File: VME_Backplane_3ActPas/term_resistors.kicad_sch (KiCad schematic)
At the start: 41 parts, among them X2H1 HI_L, X2L1 LO_L, X3H1 HI_R, X3L1 LO_R

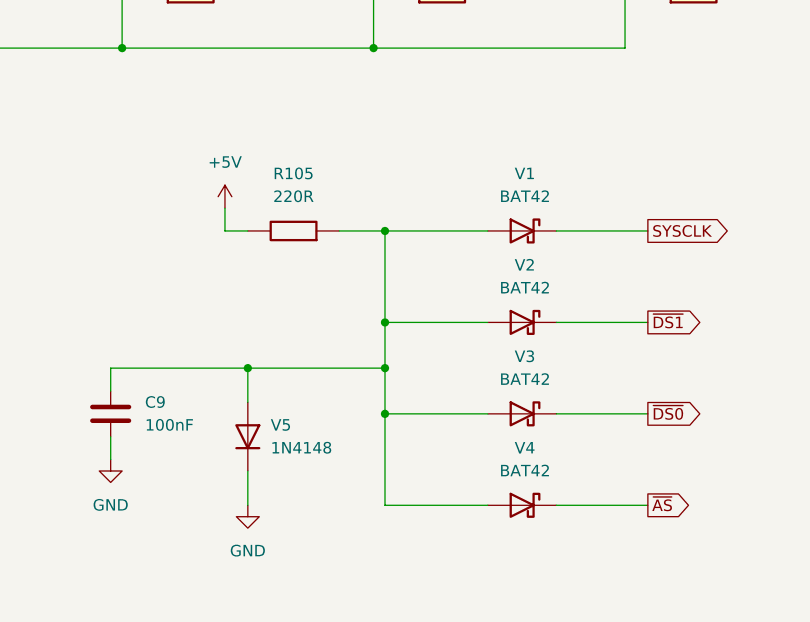
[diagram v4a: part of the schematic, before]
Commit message: Update resistor footprints with preferred silkscreen outlines
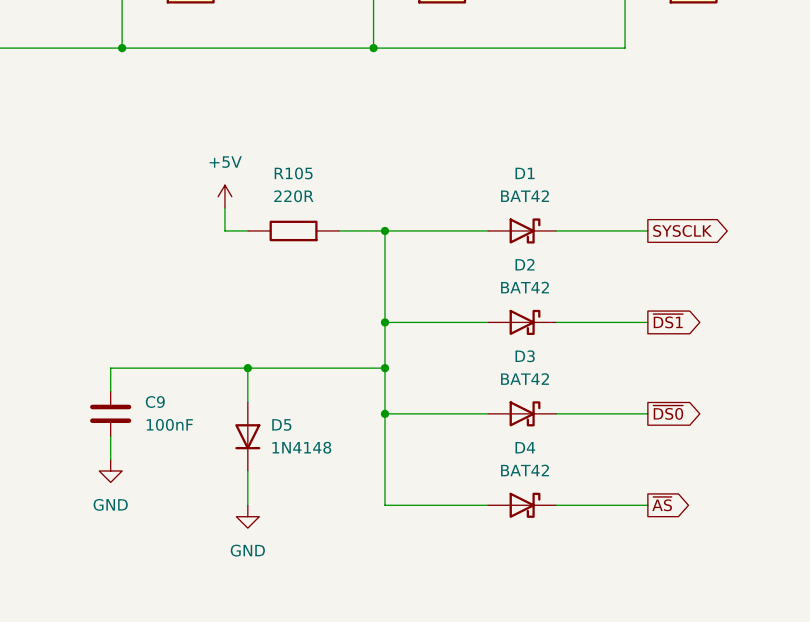
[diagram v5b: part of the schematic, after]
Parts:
- R1, R10, R11, R12, R13, R14, R15, R16, R17, R18, R2, R3, R4, R5, R6, R7, R8, R9: footprint Resistor_THT:R_Array_SIP10 -> COMET footprints:R_Array_SIP10
- R105: footprint Resistor_THT:R_Axial_DIN0207_L6.3mm_D2.5mm_P10.16mm_Horizontal -> COMET footprints:R_Axial_DIN0207_L6.3mm_D2.5mm_P10.16mm_Horizontal
- renumbered V1 to D1, V2 to D2, V3 to D3, V4 to D4, V5 to D5
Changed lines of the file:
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@@
     (property "Reference" "R14" (id 0) (at 144.78 68.58 90))
     (property "Value" "330R/470R" (id 1) (at 144.78 71.12 90))
-    (property "Footprint" "Resistor_THT:R_Array_SIP10" (id 2) (at 144.78 86.36 0)
+    (property "Footprint" "COMET footprints:R_Array_SIP10" (id 2) (at 144.78 86.36 0)
       (effects (font (size 1.27 1.27)) hide)
     )
@@
     (property "Reference" "R18" (id 0) (at 256.54 68.58 90))
     (property "Value" "330R/470R" (id 1) (at 256.54 71.12 90))
-    (property "Footprint" "Resistor_THT:R_Array_SIP10" (id 2) (at 256.54 86.36 0)
+    (property "Footprint" "COMET footprints:R_Array_SIP10" (id 2) (at 256.54 86.36 0)
       (effects (font (size 1.27 1.27)) hide)
     )
@@
     (property "Reference" "R12" (id 0) (at 88.9 68.58 90))
     (property "Value" "330R/470R" (id 1) (at 88.9 71.12 90))
-    (property "Footprint" "Resistor_THT:R_Array_SIP10" (id 2) (at 88.9 86.36 0)
+    (property "Footprint" "COMET footprints:R_Array_SIP10" (id 2) (at 88.9 86.36 0)
       (effects (font (size 1.27 1.27)) hide)
     )
@@
     (property "Reference" "R3" (id 0) (at 88.9 22.86 90))
     (property "Value" "330R/470R" (id 1) (at 88.9 25.4 90))
-    (property "Footprint" "Resistor_THT:R_Array_SIP10" (id 2) (at 88.9 40.64 0)
+    (property "Footprint" "COMET footprints:R_Array_SIP10" (id 2) (at 88.9 40.64 0)
       (effects (font (size 1.27 1.27)) hide)
     )
@@
   (symbol (lib_id "Diode:BAT42") (at 237.49 152.4 0) (mirror y) (unit 1)
     (in_bom yes) (on_board yes) (fields_autoplaced)
-    (property "Reference" "V4" (id 0) (at 237.8075 146.05 0))
+    (property "Reference" "D4" (id 0) (at 237.8075 146.05 0))
     (property "Value" "BAT42" (id 1) (at 237.8075 148.59 0))
     (property "Footprint" "Diode_THT:D_DO-35_SOD27_P10.16mm_Horizontal" (id 2) (at 237.49 156.845 0)
@@
     (property "Reference" "R5" (id 0) (at 144.78 22.86 90))
     (property "Value" "330R/470R" (id 1) (at 144.78 25.4 90))
-    (property "Footprint" "Resistor_THT:R_Array_SIP10" (id 2) (at 144.78 40.64 0)
+    (property "Footprint" "COMET footprints:R_Array_SIP10" (id 2) (at 144.78 40.64 0)
       (effects (font (size 1.27 1.27)) hide)
     )
@@
     (property "Reference" "R16" (id 0) (at 200.66 68.58 90))
     (property "Value" "330R/470R" (id 1) (at 200.66 71.12 90))
-    (property "Footprint" "Resistor_THT:R_Array_SIP10" (id 2) (at 200.66 86.36 0)
+    (property "Footprint" "COMET footprints:R_Array_SIP10" (id 2) (at 200.66 86.36 0)
       (effects (font (size 1.27 1.27)) hide)
     )
@@
     (property "Reference" "R105" (id 0) (at 212.09 115.57 90))
     (property "Value" "220R" (id 1) (at 212.09 118.11 90))
-    (property "Footprint" "Resistor_THT:R_Axial_DIN0207_L6.3mm_D2.5mm_P10.16mm_Horizontal" (id 2) (at 212.09 121.92 0)
+    (property "Footprint" "COMET footprints:R_Axial_DIN0207_L6.3mm_D2.5mm_P10.16mm_Horizontal" (id 2) (at 212.09 121.92 0)
       (effects (font (size 1.27 1.27)) hide)
     )
@@
     (property "Reference" "R4" (id 0) (at 116.84 22.86 90))
     (property "Value" "330R/470R" (id 1) (at 116.84 25.4 90))
-    (property "Footprint" "Resistor_THT:R_Array_SIP10" (id 2) (at 116.84 40.64 0)
+    (property "Footprint" "COMET footprints:R_Array_SIP10" (id 2) (at 116.84 40.64 0)
       (effects (font (size 1.27 1.27)) hide)
     )
@@
     (property "Reference" "R6" (id 0) (at 172.72 22.86 90))
     (property "Value" "330R/470R" (id 1) (at 172.72 25.4 90))
-    (property "Footprint" "Resistor_THT:R_Array_SIP10" (id 2) (at 172.72 40.64 0)
+    (property "Footprint" "COMET footprints:R_Array_SIP10" (id 2) (at 172.72 40.64 0)
       (effects (font (size 1.27 1.27)) hide)
     )
@@
   (symbol (lib_id "Diode:1N4148") (at 207.01 144.78 270) (mirror x) (unit 1)
     (in_bom yes) (on_board yes) (fields_autoplaced)
-    (property "Reference" "V5" (id 0) (at 209.55 143.5099 90)
+    (property "Reference" "D5" (id 0) (at 209.55 143.5099 90)
       (effects (font (size 1.27 1.27)) (justify left))
     )
@@
     (property "Reference" "R15" (id 0) (at 172.72 68.58 90))
     (property "Value" "330R/470R" (id 1) (at 172.72 71.12 90))
-    (property "Footprint" "Resistor_THT:R_Array_SIP10" (id 2) (at 172.72 86.36 0)
+    (property "Footprint" "COMET footprints:R_Array_SIP10" (id 2) (at 172.72 86.36 0)
       (effects (font (size 1.27 1.27)) hide)
     )
@@
     (property "Reference" "R1" (id 0) (at 33.02 22.86 90))
     (property "Value" "330R/470R" (id 1) (at 33.02 25.4 90))
-    (property "Footprint" "Resistor_THT:R_Array_SIP10" (id 2) (at 33.02 40.64 0)
+    (property "Footprint" "COMET footprints:R_Array_SIP10" (id 2) (at 33.02 40.64 0)
       (effects (font (size 1.27 1.27)) hide)
     )
@@
     (property "Reference" "R13" (id 0) (at 116.84 68.58 90))
     (property "Value" "330R/470R" (id 1) (at 116.84 71.12 90))
-    (property "Footprint" "Resistor_THT:R_Array_SIP10" (id 2) (at 116.84 86.36 0)
+    (property "Footprint" "COMET footprints:R_Array_SIP10" (id 2) (at 116.84 86.36 0)
       (effects (font (size 1.27 1.27)) hide)
     )
@@
   (symbol (lib_id "Diode:BAT42") (at 237.49 121.92 0) (mirror y) (unit 1)
     (in_bom yes) (on_board yes) (fields_autoplaced)
-    (property "Reference" "V1" (id 0) (at 237.8075 115.57 0))
+    (property "Reference" "D1" (id 0) (at 237.8075 115.57 0))
     (property "Value" "BAT42" (id 1) (at 237.8075 118.11 0))
     (property "Footprint" "Diode_THT:D_DO-35_SOD27_P10.16mm_Horizontal" (id 2) (at 237.49 126.365 0)
@@
     (property "Reference" "R17" (id 0) (at 228.6 68.58 90))
     (property "Value" "330R/470R" (id 1) (at 228.6 71.12 90))
-    (property "Footprint" "Resistor_THT:R_Array_SIP10" (id 2) (at 228.6 86.36 0)
+    (property "Footprint" "COMET footprints:R_Array_SIP10" (id 2) (at 228.6 86.36 0)
       (effects (font (size 1.27 1.27)) hide)
     )
@@
     (property "Reference" "R10" (id 0) (at 33.02 68.58 90))
     (property "Value" "330R/470R" (id 1) (at 33.02 71.12 90))
-    (property "Footprint" "Resistor_THT:R_Array_SIP10" (id 2) (at 33.02 86.36 0)
+    (property "Footprint" "COMET footprints:R_Array_SIP10" (id 2) (at 33.02 86.36 0)
       (effects (font (size 1.27 1.27)) hide)
     )
@@
     (property "Reference" "R9" (id 0) (at 256.54 22.86 90))
     (property "Value" "330R/470R" (id 1) (at 256.54 25.4 90))
-    (property "Footprint" "Resistor_THT:R_Array_SIP10" (id 2) (at 256.54 40.64 0)
+    (property "Footprint" "COMET footprints:R_Array_SIP10" (id 2) (at 256.54 40.64 0)
       (effects (font (size 1.27 1.27)) hide)
     )
@@
     (property "Reference" "R11" (id 0) (at 60.96 68.58 90))
     (property "Value" "330R/470R" (id 1) (at 60.96 71.12 90))
-    (property "Footprint" "Resistor_THT:R_Array_SIP10" (id 2) (at 60.96 86.36 0)
+    (property "Footprint" "COMET footprints:R_Array_SIP10" (id 2) (at 60.96 86.36 0)
       (effects (font (size 1.27 1.27)) hide)
     )
@@
     (property "Reference" "R2" (id 0) (at 60.96 22.86 90))
     (property "Value" "330R/470R" (id 1) (at 60.96 25.4 90))
-    (property "Footprint" "Resistor_THT:R_Array_SIP10" (id 2) (at 60.96 40.64 0)
+    (property "Footprint" "COMET footprints:R_Array_SIP10" (id 2) (at 60.96 40.64 0)
       (effects (font (size 1.27 1.27)) hide)
     )
@@
   (symbol (lib_id "Diode:BAT42") (at 237.49 142.24 0) (mirror y) (unit 1)
     (in_bom yes) (on_board yes) (fields_autoplaced)
-    (property "Reference" "V3" (id 0) (at 237.8075 135.89 0))
+    (property "Reference" "D3" (id 0) (at 237.8075 135.89 0))
     (property "Value" "BAT42" (id 1) (at 237.8075 138.43 0))
     (property "Footprint" "Diode_THT:D_DO-35_SOD27_P10.16mm_Horizontal" (id 2) (at 237.49 146.685 0)
@@
   (symbol (lib_id "Diode:BAT42") (at 237.49 132.08 0) (mirror y) (unit 1)
     (in_bom yes) (on_board yes) (fields_autoplaced)
-    (property "Reference" "V2" (id 0) (at 237.8075 125.73 0))
+    (property "Reference" "D2" (id 0) (at 237.8075 125.73 0))
     (property "Value" "BAT42" (id 1) (at 237.8075 128.27 0))
     (property "Footprint" "Diode_THT:D_DO-35_SOD27_P10.16mm_Horizontal" (id 2) (at 237.49 136.525 0)
@@
     (property "Reference" "R7" (id 0) (at 200.66 22.86 90))
     (property "Value" "330R/470R" (id 1) (at 200.66 25.4 90))
-    (property "Footprint" "Resistor_THT:R_Array_SIP10" (id 2) (at 200.66 40.64 0)
+    (property "Footprint" "COMET footprints:R_Array_SIP10" (id 2) (at 200.66 40.64 0)
       (effects (font (size 1.27 1.27)) hide)
     )
@@
     (property "Reference" "R8" (id 0) (at 228.6 22.86 90))
     (property "Value" "330R/470R" (id 1) (at 228.6 25.4 90))
-    (property "Footprint" "Resistor_THT:R_Array_SIP10" (id 2) (at 228.6 40.64 0)
-      (effects (font (size 1.27 1.27)) hide)
-    )
+    (property "Footprint" "COMET footprints:R_Array_SIP10" (id 2) (at 228.6 40.64 0)
+      (effects (font (size 1.27 1.27)) hide)
+    )
